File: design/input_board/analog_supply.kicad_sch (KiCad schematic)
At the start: 24 parts, among them IC10 LM5157RTER, U2 TPS7A4701xRGW, U5 INA180

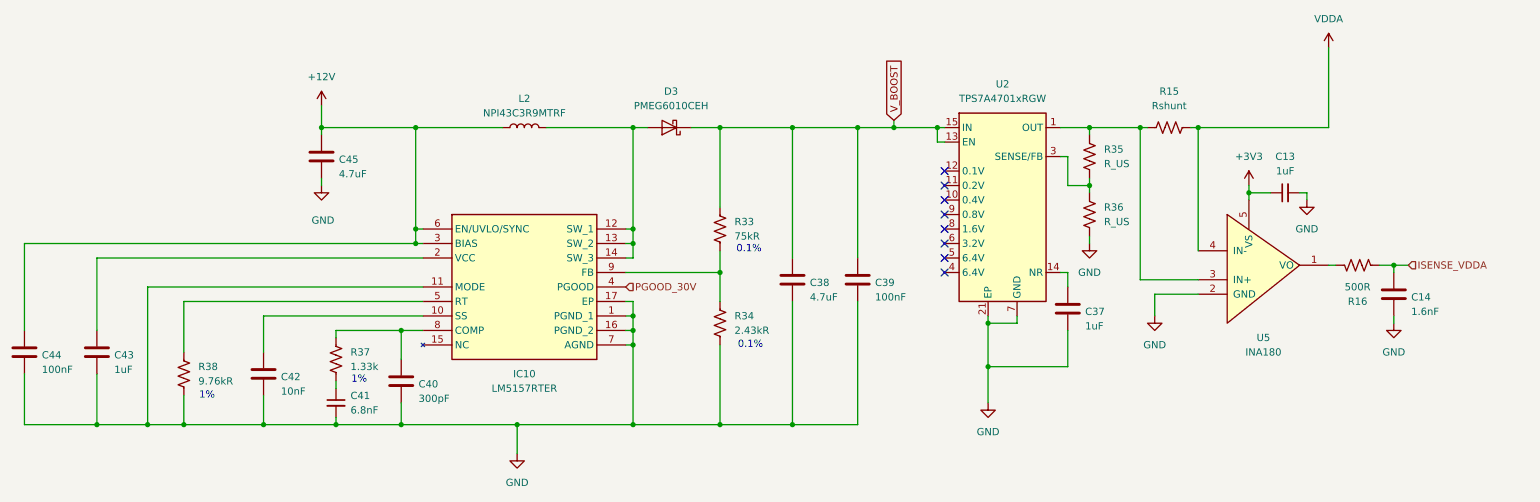
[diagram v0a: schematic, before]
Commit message: Finihs schamtic and footprints; DVDD 3.3->2V
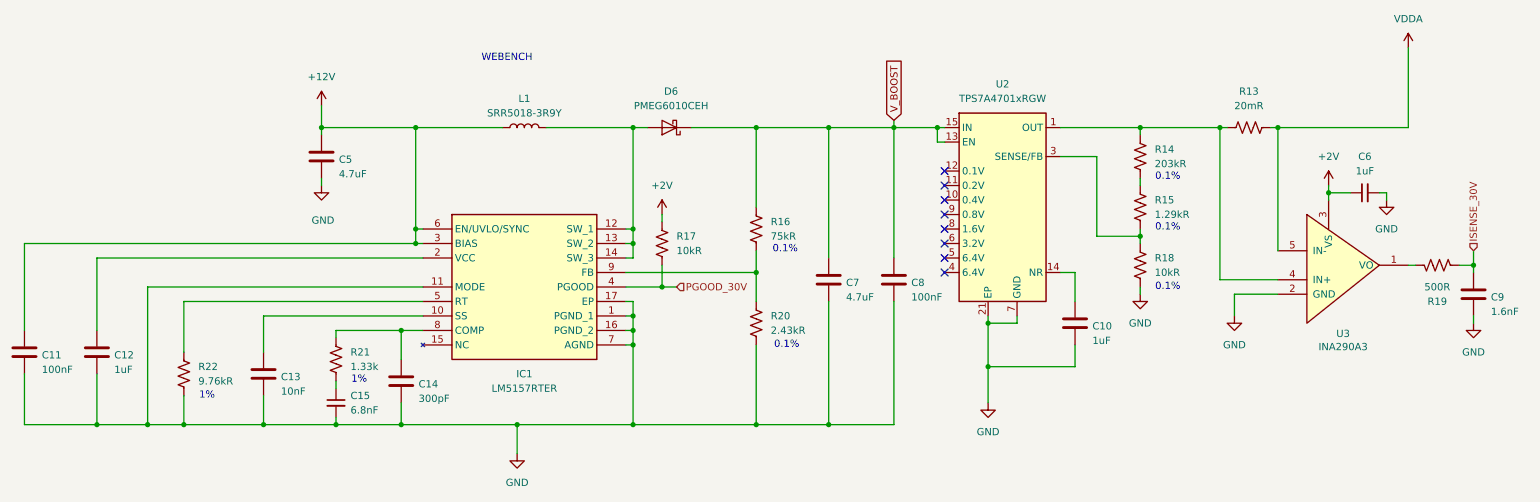
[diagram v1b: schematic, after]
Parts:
- removed U5: INA180, symbol canhw:INA180
- added R15: 1.29kR, Resistor_SMD:R_0805_2012Metric_Pad1.20x1.40mm_HandSolder, symbol Device:R_US
- added R17: 10kR, Resistor_SMD:R_0805_2012Metric_Pad1.20x1.40mm_HandSolder, symbol Device:R_US
- added U3: INA290A3, input_board:SC70-5_DCK_TEX, symbol canhw:INA180
- C15: renamed from C41; footprint (none) -> Capacitor_SMD:C_0805_2012Metric_Pad1.18x1.45mm_HandSolder
- C6: renamed from C13; footprint (none) -> Capacitor_SMD:C_0805_2012Metric_Pad1.18x1.45mm_HandSolder
- IC1: renamed from IC10; footprint QFN50P300X300X80-17N-D -> input_board:QFN50P300X300X80-17N-D
- L1: renamed from L2; value NPI43C3R9MTRF -> SRR5018-3R9Y; footprint (none) -> input_board:IND_BOURNS_SRR5018
- R13: renamed from R15; value Rshunt -> 20mR; footprint (none) -> Resistor_SMD:R_0805_2012Metric_Pad1.20x1.40mm_HandSolder
- R14: renamed from R35; value R_US -> 203kR; footprint (none) -> Resistor_SMD:R_0805_2012Metric_Pad1.20x1.40mm_HandSolder
- R16: renamed from R33; footprint (none) -> Resistor_SMD:R_0805_2012Metric_Pad1.20x1.40mm_HandSolder
- R18: renamed from R36; value R_US -> 10kR; footprint (none) -> Resistor_SMD:R_0805_2012Metric_Pad1.20x1.40mm_HandSolder
- R20: renamed from R34; footprint (none) -> Resistor_SMD:R_0805_2012Metric_Pad1.20x1.40mm_HandSolder
- R21: renamed from R37; footprint (none) -> Resistor_SMD:R_0805_2012Metric_Pad1.20x1.40mm_HandSolder
- R22: renamed from R38; footprint (none) -> Resistor_SMD:R_0805_2012Metric_Pad1.20x1.40mm_HandSolder
- renumbered C37 to C10, C44 to C11, C43 to C12, C42 to C13, C40 to C14, C45 to C5, C38 to C7, C39 to C8, C14 to C9, D3 to D6, R16 to R19
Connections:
- net GND: now also U3.2 (GND)
- net PGOOD_30V: now also R17.2
- net VDDA: now also U3.5 (IN-)
- net at R19.2: now also U3.1 (VO)
- net at R13.1, R14.1, U2.1 (OUT)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: now also U3.4 (IN+)
- net at R18.1, U2.3 (SENSE/FB): now also R15.2; no longer R14.2
- net +3V3 renamed +2V
- net +2V: now also R17.1, U3.3 (VS)
- net ISENSE_VDDA renamed ISENSE_30V
- new net: R14.2, R15.1
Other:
- note added: "WEBENCH"
- moved on the sheet: C10, C6, C7, C8, C9, R13, R14, R16, R18, R19, R20

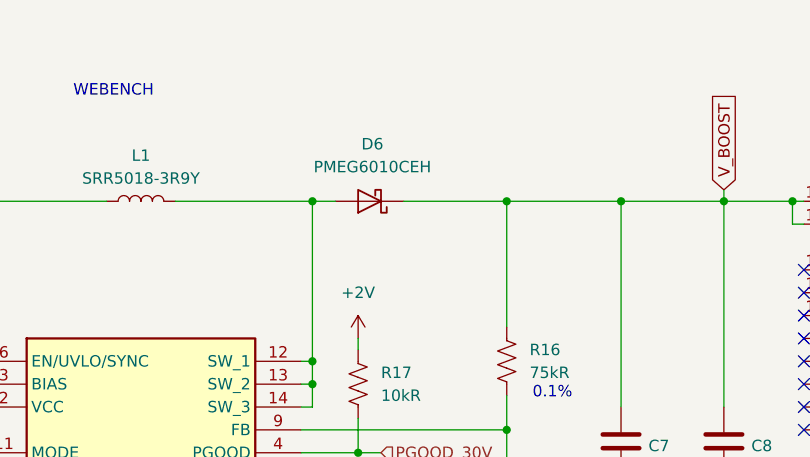
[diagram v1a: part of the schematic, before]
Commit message: Layout v1, its bad
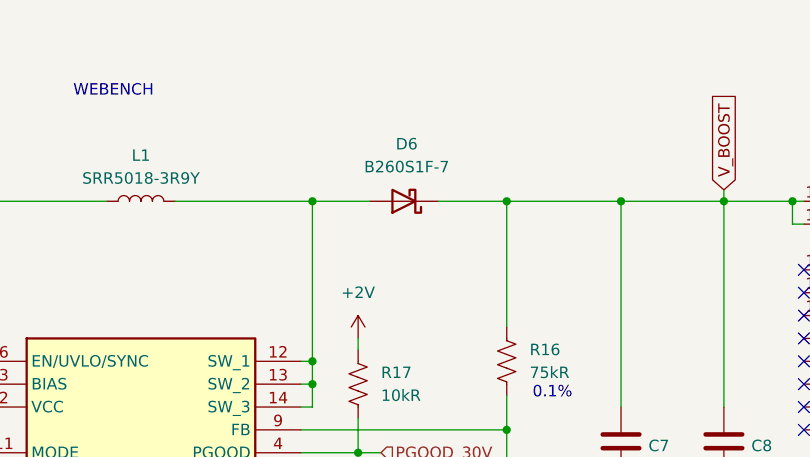
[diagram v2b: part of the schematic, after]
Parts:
- removed D6: PMEG6010CEH, Diode_SMD:D_SOD-123F, symbol Diode:PMEG6010CEH
- added D6: B260S1F-7, input_board:CR_SOD123F_DIO, symbol Device:D_Schottky
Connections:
- net V_BOOST: now also D6.1 (K)
- net at IC1.12 (SW_1), IC1.13 (SW_2), IC1.14 (SW_3)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: now also D6.2 (A)
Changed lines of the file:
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@@
 	(wire
 		(pts
-			(xy 138.43 57.15) (xy 149.86 57.15)
+			(xy 142.24 57.15) (xy 149.86 57.15)
 		)
 		(stroke
@@
 	(wire
 		(pts
-			(xy 128.27 57.15) (xy 130.81 57.15)
+			(xy 128.27 57.15) (xy 134.62 57.15)
 		)
 		(stroke
@@
 	)
 	(symbol
+		(lib_id "Device:D_Schottky")
+		(at 138.43 57.15 180)
+		(unit 1)
+		(exclude_from_sim no)
+		(in_bom yes)
+		(on_board yes)
+		(dnp no)
+		(fields_autoplaced yes)
+		(property "Reference" "D6"
+			(at 138.7475 50.8 0)
+			(effects
+				(font
+					(size 1.27 1.27)
+				)
+			)
+		)
+		(property "Value" "B260S1F-7"
+			(at 138.7475 53.34 0)
+			(effects
+				(font
+					(size 1.27 1.27)
+				)
+			)
+		)
+		(property "Footprint" "input_board:CR_SOD123F_DIO"
+			(at 138.43 57.15 0)
+			(effects
+				(font
+					(size 1.27 1.27)
+				)
+				(hide yes)
+			)
+		)
+		(property "Datasheet" "~"
+			(at 138.43 57.15 0)
+			(effects
+				(font
+					(size 1.27 1.27)
+				)
+				(hide yes)
+			)
+		)
+		(property "Description" "Schottky diode"
+			(at 138.43 57.15 0)
+			(effects
+				(font
+					(size 1.27 1.27)
+				)
+				(hide yes)
+			)
+		)
+		(pin "1"
+		)
+		(pin "2"
+		)
+		(instances
+			(project ""
+				(path "/edc2dfd5-6e83-475f-94b9-1e03bbedf967/a604fd4b-db33-4b34-9705-31ee8512e06a"
+					(reference "D6")
+					(unit 1)
+				)
+			)
+		)
+	)
+	(symbol
 		(lib_id "power:+12V")
 		(at 73.66 53.34 0)
@@
 					(unit 1)
 				)
-			)
-		)
-	)
-	(symbol
-		(lib_id "Diode:PMEG6010CEH")
-		(at 134.62 57.15 180)
-		(unit 1)
-		(exclude_from_sim no)
-		(in_bom yes)
-		(on_board yes)
-		(dnp no)
-		(fields_autoplaced yes)
-		(property "Reference" "D6"
-			(at 134.9375 50.8 0)
-			(effects
-				(font
-					(size 1.27 1.27)
-				)
-			)
-		)
-		(property "Value" "PMEG6010CEH"
-			(at 134.9375 53.34 0)
-			(effects
-				(font
-					(size 1.27 1.27)
-				)
-			)
-		)
-		(property "Footprint" "Diode_SMD:D_SOD-123F"
-			(at 134.62 52.705 0)
-			(effects
-				(font
-					(size 1.27 1.27)
-				)
-				(hide yes)
-			)
-		)
-		(property "Datasheet" "https://assets.nexperia.com/documents/data-sheet/PMEG6010CEH_PMEG6010CEJ.pdf"
-			(at 134.62 57.15 0)
-			(effects
-				(font
-					(size 1.27 1.27)
-				)
-				(hide yes)
-			)
-		)
-		(property "Description" "60V, 1A very low Vf MEGA Schottky barrier rectifier, SOD-123F"
-			(at 134.62 57.15 0)
-			(effects
-				(font
-					(size 1.27 1.27)
-				)
-				(hide yes)
-			)
-		)
-		(pin "2"
-		)
-		(pin "1"
-		)
-		(instances
-			(project ""
-				(path "/edc2dfd5-6e83-475f-94b9-1e03bbedf967/a604fd4b-db33-4b34-9705-31ee8512e06a"
-					(reference "D6")
-					(unit 1)
-				)
